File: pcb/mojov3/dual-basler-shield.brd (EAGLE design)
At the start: 78.7 x 63.5 mm, 19 parts

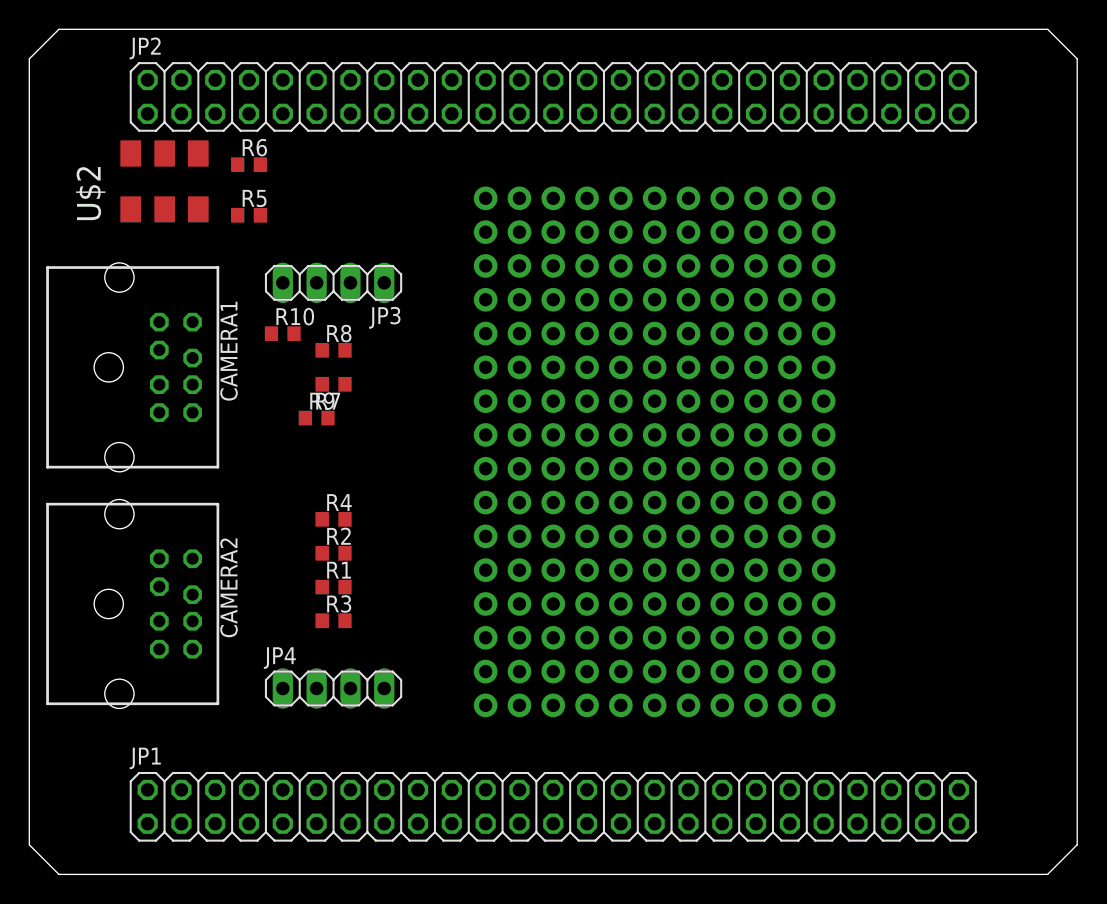
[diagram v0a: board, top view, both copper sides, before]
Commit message: dual basler shield circuit complete
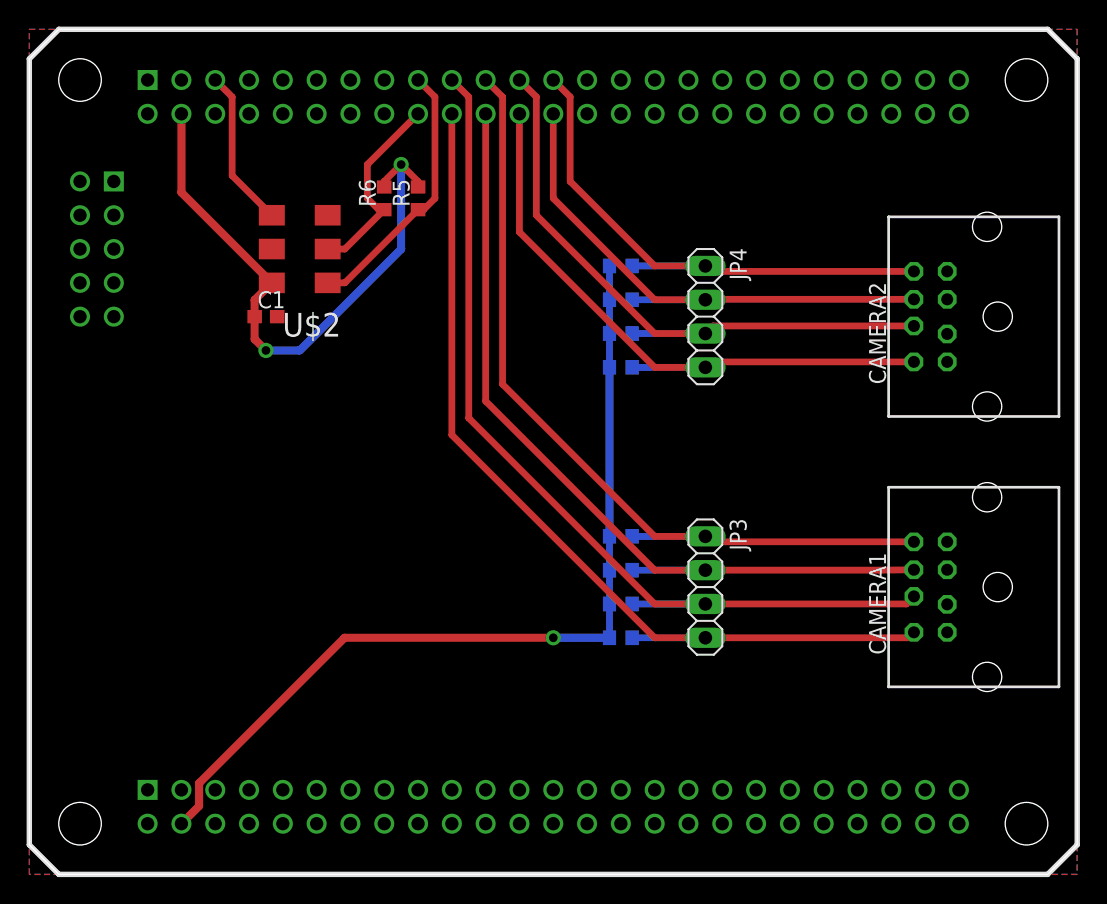
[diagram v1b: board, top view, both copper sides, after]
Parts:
- removed JP1, JP2: (no value), pinhead:2X25
- removed U$1: 12X16PERF, custom-regs:PERF-GRID
- added C1: (no value), rcl:C0603
- added U$4: MOJOV3, EmbeddedMicro-Mojo:MOJO_V3
- moved CAMERA2 79.2 mm to (77.5, 41.9), turned to 90 degrees
- moved CAMERA1 78.0 mm to (77.5, 21.6), turned to 90 degrees
- moved JP4 39.5 mm to (50.8, 41.9), turned to 270 degrees
- moved JP3 36.1 mm to (50.8, 21.6), turned to 270 degrees
- moved R3 34.3 mm to (44.5, 45.7), flipped to the bottom
- moved R10 34.2 mm to (44.5, 17.8), flipped to the bottom
- moved R1 30.5 mm to (44.5, 43.2), flipped to the bottom
- moved R8 28.8 mm to (44.5, 20.3), flipped to the bottom
- moved R2 27.2 mm to (44.5, 40.6), flipped to the bottom
- moved R7 25.7 mm to (44.5, 22.9), flipped to the bottom, turned to 0 degrees
- moved R9 24.5 mm to (44.5, 25.4), flipped to the bottom
- moved R4 24.4 mm to (44.5, 38.1), flipped to the bottom
- moved R5 12.8 mm to (29.2, 50.8), turned to 90 degrees
- moved U$2 11.4 mm to (20.3, 47.0), turned to 180 degrees
- moved R6 10.5 mm to (26.7, 50.8), turned to 90 degrees
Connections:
- removed net GND1: U$2.P$3
- new net VDD: C1.1, R5.2, R6.2, U$2.P$6, U$4.V@1
- net 3V3: now also U$4.V@2; no longer JP2.3, R5.2, R6.2, U$2.P$6
- net CLK: now also U$4.51; no longer JP2.6
- net GND: now also C1.2, U$2.P$3, U$4.GND@1, U$4.GND@2, U$4.GND@3, U$4.GND@4; no longer JP1.2, JP1.4, JP2.2, JP2.4
- net LINE_1_1: now also U$4.17; no longer JP2.12
- net LINE_1_2: now also U$4.16; no longer JP2.11
- net LINE_1_3: now also U$4.22; no longer JP2.10
- net LINE_1_4: now also U$4.21; no longer JP2.9
- net LINE_2_1: now also U$4.12
- net LINE_2_2: now also U$4.11
- net LINE_2_3: now also U$4.15
- net LINE_2_4: now also U$4.14
- net SCL: now also U$4.23; no longer JP2.7
- net SDA: now also U$4.24; no longer JP2.8
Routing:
- net LINE_1_3: track 0.00 -> 70.9 mm
- net LINE_1_4: track 0.00 -> 70.8 mm
- net 3V3: track 0.00 -> 66.9 mm, vias 0 -> 1
- net LINE_1_1: track 0.00 -> 64.7 mm
- net LINE_1_2: track 0.00 -> 64.5 mm
- net LINE_2_3: track 0.00 -> 48.5 mm
- net LINE_2_4: track 0.00 -> 48.4 mm
- net VDD: track 0.00 -> 45.6 mm, vias 0 -> 2
- net LINE_2_1: track 0.00 -> 42.3 mm
- net LINE_2_2: track 0.00 -> 42.1 mm
- net SDA: track 0.00 -> 20.1 mm
- net SCL: track 0.00 -> 15.0 mm
- net CLK: track 0.00 -> 11.9 mm
- added copper zone on layer 1, net GND
- added copper zone on layer 16, net GND

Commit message: dual basler shield silkscreen edit
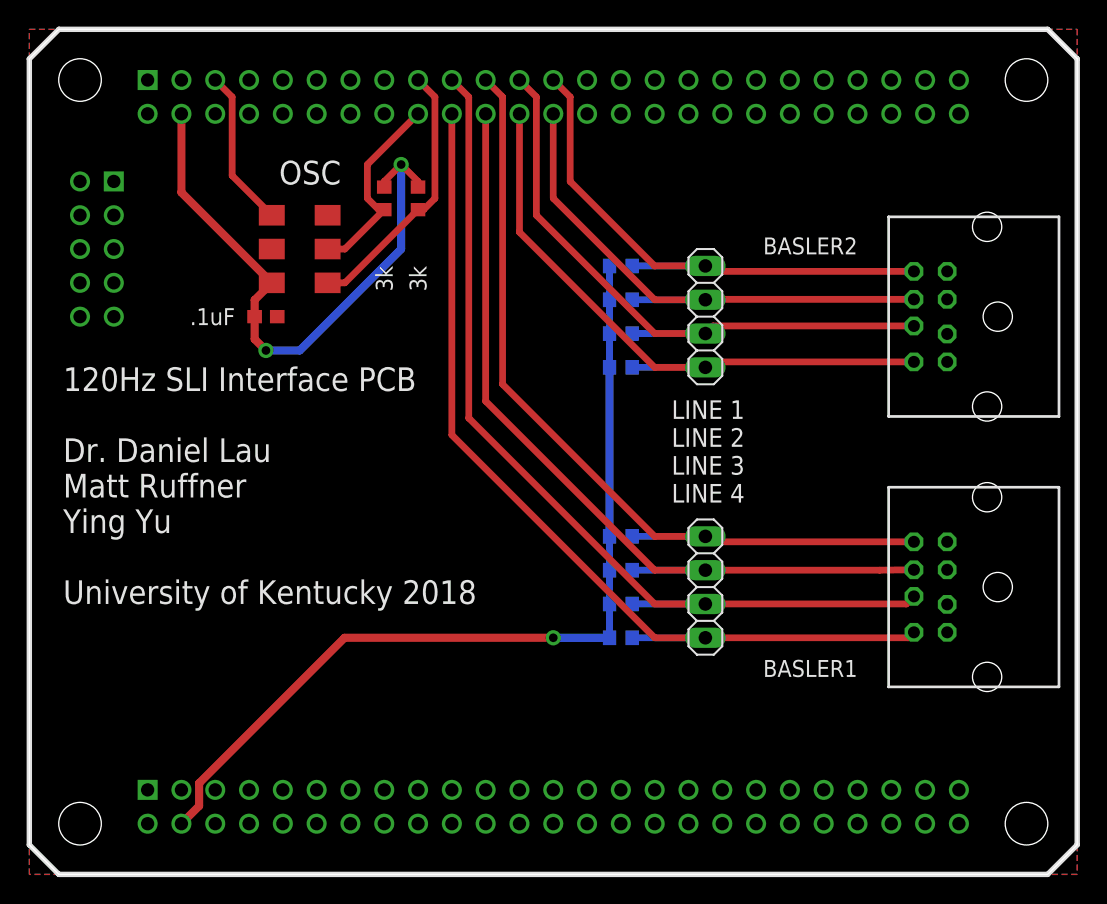
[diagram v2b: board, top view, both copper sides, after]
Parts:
- C1: value (none) -> .1uF
- R1, R10, R2, R3, R4, R7, R8, R9: value (none) -> 1k
- R5, R6: value (none) -> 3k
- renumbered CAMERA1 to BASLER1, CAMERA2 to BASLER2, U$2 to OSC
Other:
- board text added: "120Hz SLI Interface PCB Dr. Daniel Lau Matt Ruffner Ying Yu University of Kentucky 2018"
- board text added: "LINE 1 LINE 2 LINE 3 LINE 4"
